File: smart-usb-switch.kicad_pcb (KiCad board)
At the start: 2 copper layers, 50.8 x 20.3 mm, 8 parts, among them J1 USB_A, J2 USB_A, J3 Conn_01x04, J4 Conn_01x02, Q1 2N7002E, U1 ESP-12F, U2 TLV75533PDBV

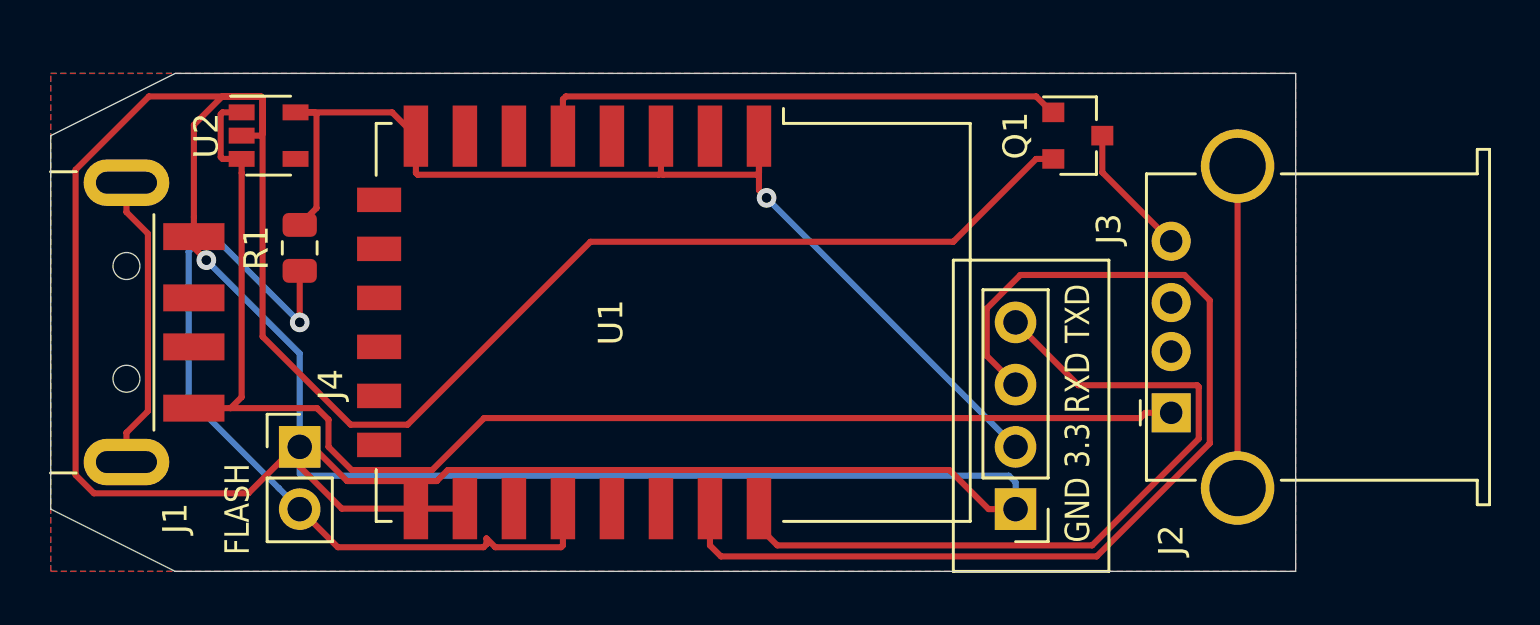
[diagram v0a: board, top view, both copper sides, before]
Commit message: Fix #1: switch to GPIO4
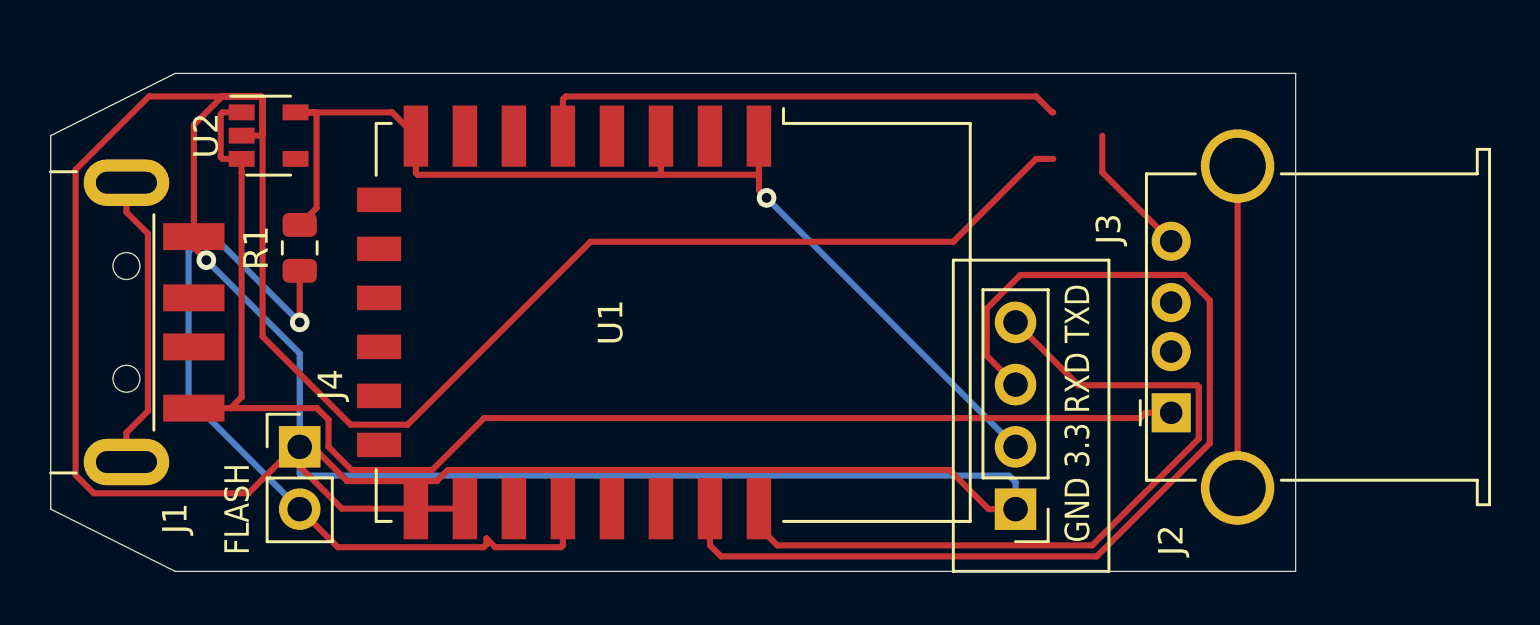
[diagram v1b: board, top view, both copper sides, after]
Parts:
- removed Q1: 2N7002E, Package_TO_SOT_SMD:SOT-23
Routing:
- removed copper zone on B.Cu, net GND
- removed copper zone on F.Cu, net GND

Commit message: more docs, updates
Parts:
- added Q1: 2N7002E, Package_TO_SOT_SMD:SOT-23, F.Cu at (148.6, 86.4)
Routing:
- net GND: track 170.4 -> 79.8 mm, vias 1 -> 3
- net Net-(Q1-Pad1): track 0.00 -> 27.0 mm, vias 0 -> 2
- net Net-(U1-Pad5): track 21.8 -> 0.00 mm
- added copper zone on B.Cu, net GND
- added copper zone on F.Cu, net GND

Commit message: reroute
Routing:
- net Net-(J3-Pad3): track 43.5 -> 15.5 mm
- net Net-(J3-Pad4): track 31.5 -> 17.3 mm
- net GND: track 79.8 -> 68.1 mm, vias 3 -> 1
- net +3V3: track 46.6 -> 57.8 mm, vias 1 -> 0
- net Net-(J4-Pad2): track 33.9 -> 25.1 mm, vias 1 -> 0
- net VBUS: track 56.4 -> 61.1 mm
- net Net-(Q1-Pad1): track 27.0 -> 25.6 mm, vias 2 -> 0
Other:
- board text added: "GPIO 4 controls USB power"
- board text added: "github.com/sowbug/smart-usb-switch"
- board text removed: "GPIO 14 controls USB power"
